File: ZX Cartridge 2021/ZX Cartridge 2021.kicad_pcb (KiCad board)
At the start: 2 copper layers, 57.9 x 61.6 mm, 10 parts, among them J1 Cartridge, M1 Mounting, M2 Mounting, M3 Mounting, M4 Mounting, U1 27C512, U2 27C512

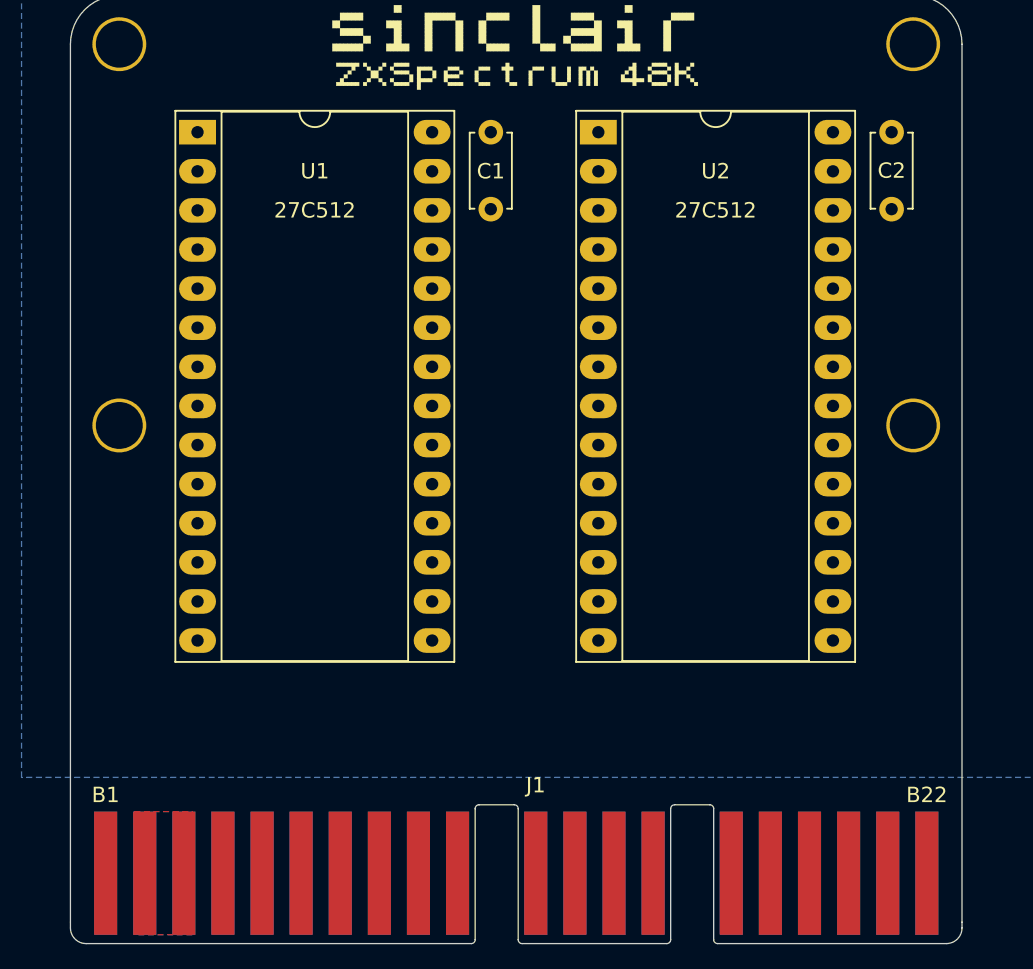
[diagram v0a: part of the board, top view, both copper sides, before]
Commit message: 27c512 cartridge layout done
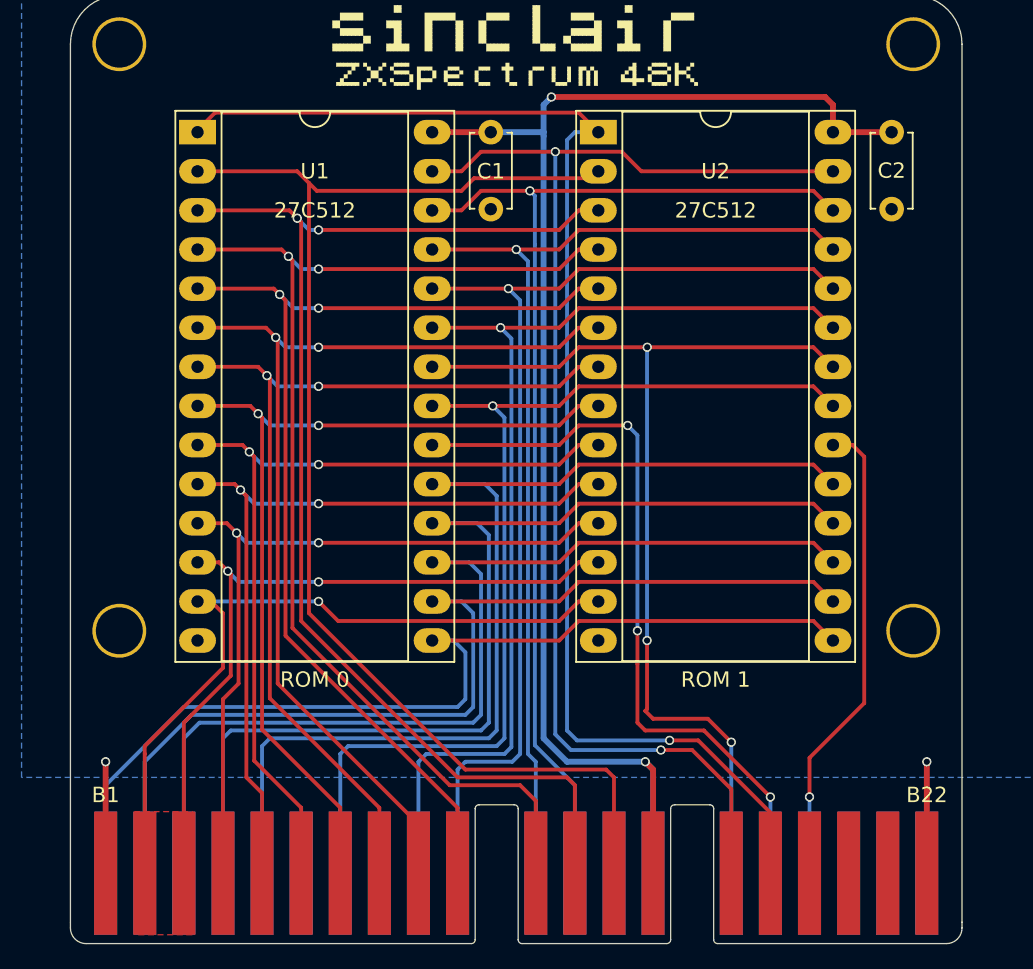
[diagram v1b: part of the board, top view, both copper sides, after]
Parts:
- added sinclair_title: , artwork:sinclair_title, B.Cu at (161.5, 59.7)
- moved M1 13.3 mm to (123.4, 100.3)
- moved M2 13.3 mm to (175.0, 100.3)
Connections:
- J1 pad A19: (no net) -> /~ROM_1
- U2 pad 20: /~ROM_0 -> /~ROM_1
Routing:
- net VCC: track 0.00 -> 95.3 mm, vias 0 -> 2
- net /BA15: track 0.00 -> 87.1 mm, vias 0 -> 1
- net /A12: track 0.00 -> 85.5 mm
- net /BA14: track 0.00 -> 83.3 mm, vias 0 -> 2
- net /A7: track 0.00 -> 81.3 mm, vias 0 -> 2
- net /A6: track 0.00 -> 76.5 mm, vias 0 -> 2
- net /A13: track 0.00 -> 72.6 mm, vias 0 -> 1
- net /D7: track 0.00 -> 70.7 mm
- net /D6: track 0.00 -> 69.7 mm
- net /A5: track 0.00 -> 69.5 mm, vias 0 -> 2
- net /A9: track 0.36 -> 69.2 mm, vias 0 -> 1
- net /D5: track 0.00 -> 68.4 mm
- net /A11: track 0.00 -> 68.3 mm, vias 0 -> 1
- net /A8: track 0.00 -> 68.1 mm, vias 0 -> 1
- net /A10: track 0.00 -> 67.8 mm, vias 0 -> 1
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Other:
- board text added: "ROM 0"
- board text added: "ROM 1"

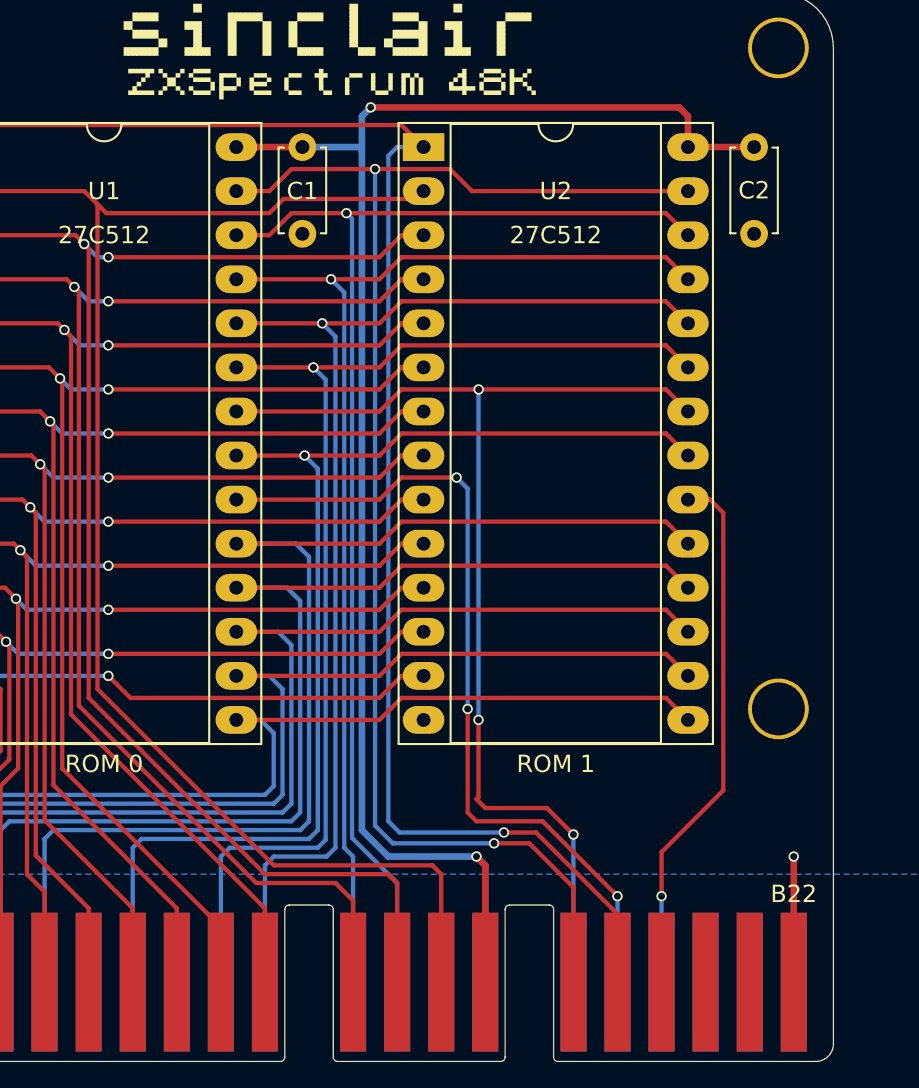
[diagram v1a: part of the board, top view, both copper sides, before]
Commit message: Added 27C256 and 27C128 compatibility
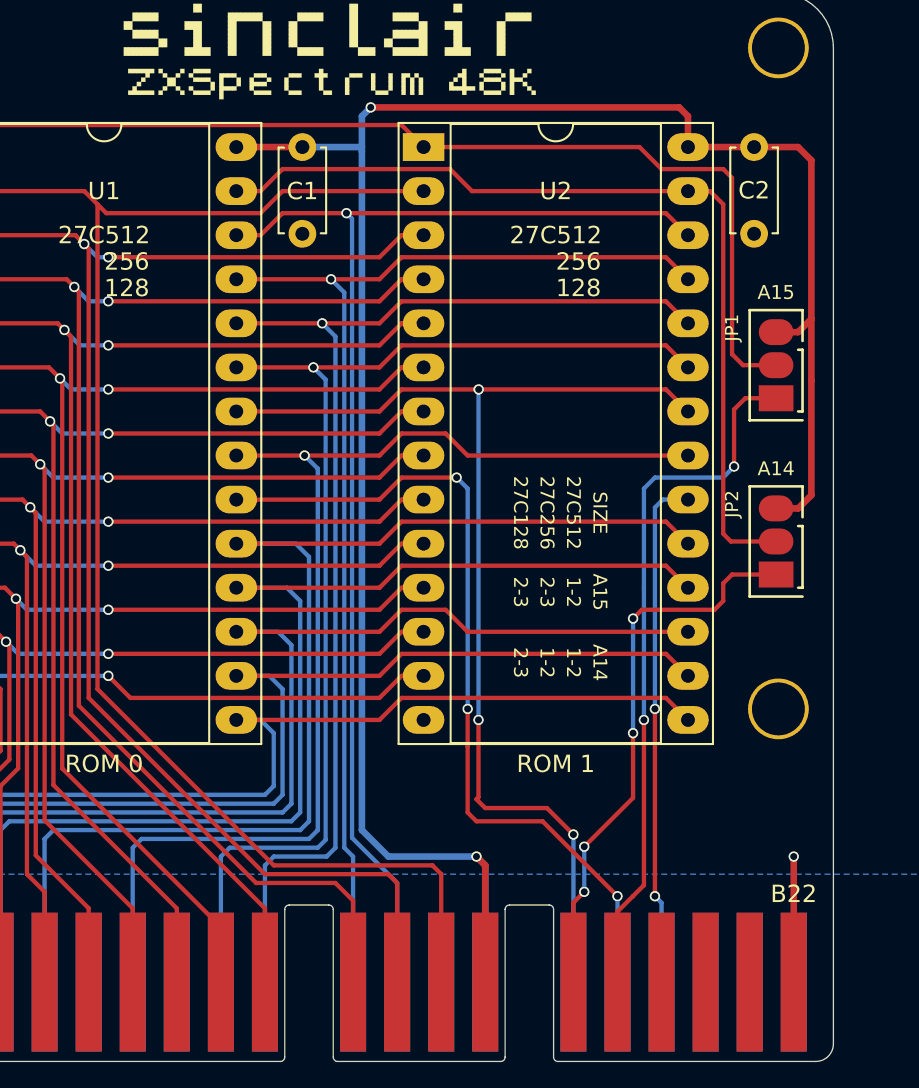
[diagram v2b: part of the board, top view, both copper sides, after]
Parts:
- added JP1: A15, solder_bridge:select, F.Cu at (174.9, 82.4)
- added JP2: A14, solder_bridge:select, F.Cu at (174.9, 92.6)
- moved sinclair_title 0.13 mm to (161.7, 59.7)
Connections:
- J1 pad B17: /BA14 -> Net-(J1-PadB17)
- J1 pad B18: /BA15 -> Net-(J1-PadB18)
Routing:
- net Net-(J1-PadB18): track 0.00 -> 40.8 mm, vias 0 -> 2
- net Net-(J1-PadB17): track 0.00 -> 32.3 mm, vias 0 -> 4
- net /BA14: track 83.3 -> 51.7 mm, vias 2 -> 0
- net /BA15: track 87.1 -> 58.6 mm, vias 1 -> 0
- net VCC: track 95.3 -> 122.9 mm
- net /~ROM_1: track 30.9 -> 29.6 mm, vias 1 -> 2
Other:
- board text added: "1-2"
- board text added: "128"
- board text added: "2-3"
- board text added: "256"
- board text added: "27C128"
- board text added: "27C256"
- board text added: "27C512"
- board text added: "A14"
- board text added: "A15"
- board text added: "SIZE"

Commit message: Added grip
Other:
- outline, holes or cut-outs redrawn
